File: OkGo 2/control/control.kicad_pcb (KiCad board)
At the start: 2 copper layers, 92.2 x 64.5 mm, 69 parts, among them M3_MOUNT VAL**, P102 KEYSW, P105 BATT, P106 ARM_LED, P108 SMA, P110 POWER_SW, P111 SERIAL, P201 CH1, P202 CH2, P205 CH3, P206 CH4, Q201 BSS138BK, Q202 BSS138BK, Q203 BSS138BK, Q204 BSS138BK, U101 SWD, U102 STM32F071CBT6, U103 MEJ2S0305SC, U105 RFM95W, U106 LCD_HD44780, U107 ADP3335, Y101 8MHz

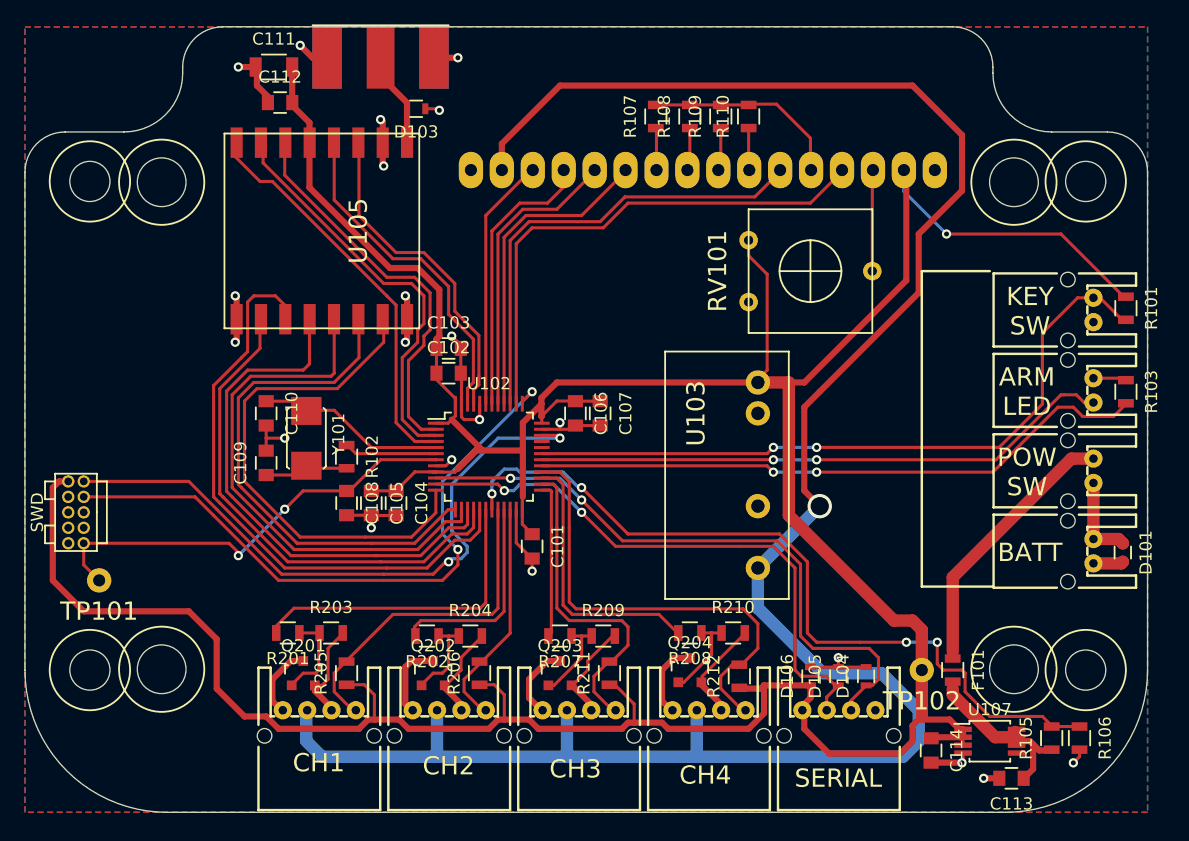
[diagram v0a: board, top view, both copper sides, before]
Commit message: Fixed #28 on control
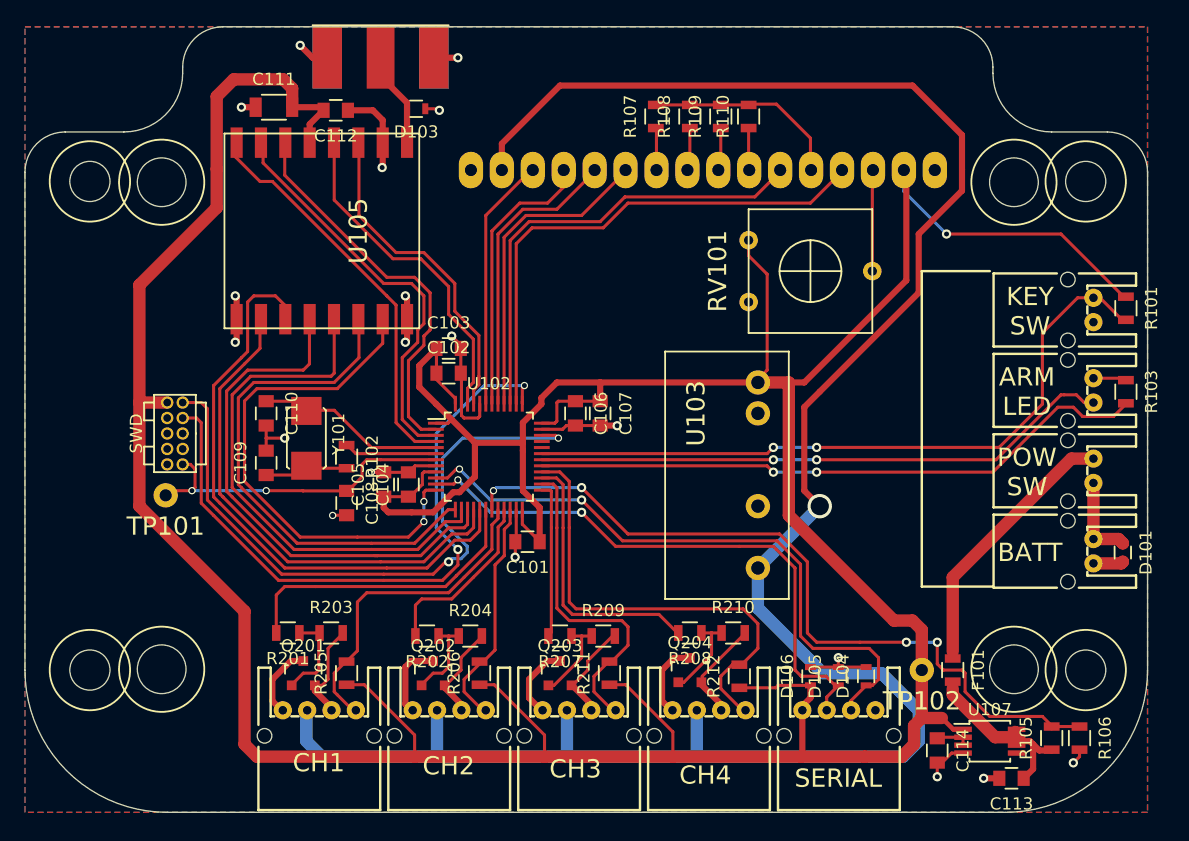
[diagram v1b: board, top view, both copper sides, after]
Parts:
- moved U101 10.4 mm to (145.5, 98.4)
- moved TP101 8.87 mm to (144.1, 106.0)
- moved C112 4.62 mm to (158.1, 74.4), turned to 180 degrees
- moved C111 3.30 mm to (153.0, 74.2)
- moved C104 1.83 mm to (164.1, 105.2), turned to 90 degrees
- moved C105 1.83 mm to (162.1, 105.2), turned to 90 degrees
- moved C101 0.54 mm to (173.9, 109.9), turned to 180 degrees
- moved C114 0.51 mm to (207.5, 127.0)
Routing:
- net +3V3: track 313.8 -> 360.6 mm
- net /nRST: track 36.4 -> 27.4 mm
- net /controls/CH2_LED: track 17.0 -> 15.1 mm
- net /BATT_MON: track 65.9 -> 64.4 mm
- net /SWDCLK: track 53.2 -> 54.7 mm
- net /SWDIO: track 53.6 -> 54.6 mm
- net /controls/CH1_SW: track 27.8 -> 27.1 mm
- net /controls/CH1_LED: track 26.3 -> 25.6 mm
- net /RFM_DIO5: track 42.5 -> 43.1 mm, vias 0 -> 2
- net Net-(D104-Pad1): track 51.5 -> 52.1 mm
- net GND: track 119.3 -> 118.8 mm, vias 21 -> 19

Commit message: Tidied control 3v3,5 fixes #38
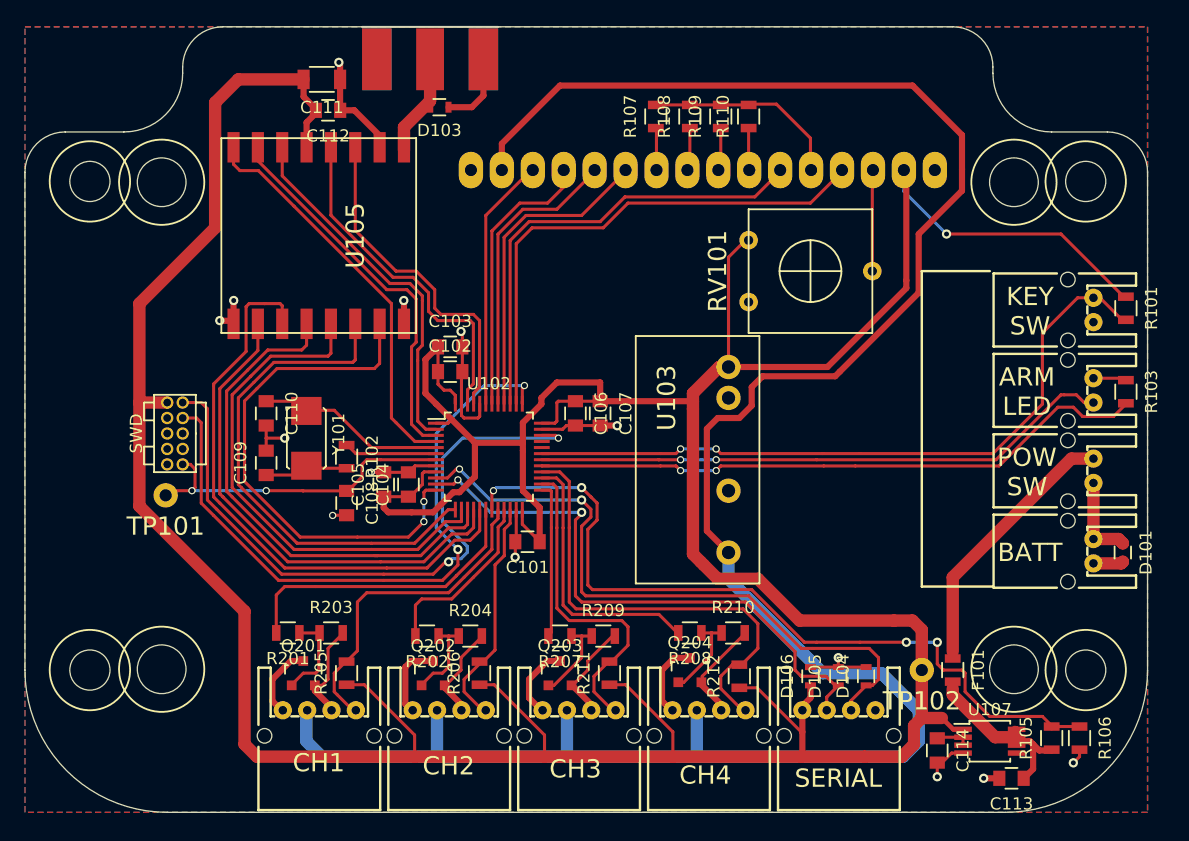
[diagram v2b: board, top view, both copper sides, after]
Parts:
- moved C111 4.55 mm to (157.0, 71.9), turned to 180 degrees
- moved P108 4.07 mm to (165.9, 70.2)
- moved U103 2.73 mm to (190.4, 95.5)
- moved D103 1.91 mm to (166.6, 74.2)
- moved C112 0.64 mm to (157.5, 74.4)
- moved U105 0.46 mm to (156.7, 84.7)
- moved C103 0.18 mm to (167.5, 93.9)
- moved C102 0.18 mm to (167.5, 95.9)
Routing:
- net +3V3: track 360.6 -> 368.4 mm
- net +5V: track 175.2 -> 182.8 mm, vias 1 -> 0
- net /RFM_DIO0: track 32.7 -> 29.9 mm
- net /RFM_DIO1: track 33.4 -> 31.4 mm
- net /RFM_NSS: track 44.3 -> 42.7 mm
- net /BATT_MON: track 64.4 -> 66.0 mm
- net Net-(D104-Pad1): track 52.1 -> 53.7 mm
- net /RFM_SCK: track 44.4 -> 42.9 mm
- net GND: track 118.8 -> 117.6 mm, vias 19 -> 14
- net /RFM_DIO2: track 33.5 -> 32.7 mm
- net /RFM_DIO3: track 27.0 -> 27.8 mm
- net /RFM_MOSI: track 49.1 -> 48.4 mm
- net Net-(D105-Pad1): track 47.5 -> 48.3 mm
- net Net-(D103-Pad2): track 8.19 -> 8.88 mm
- net /RFM_RESET: track 42.8 -> 42.2 mm

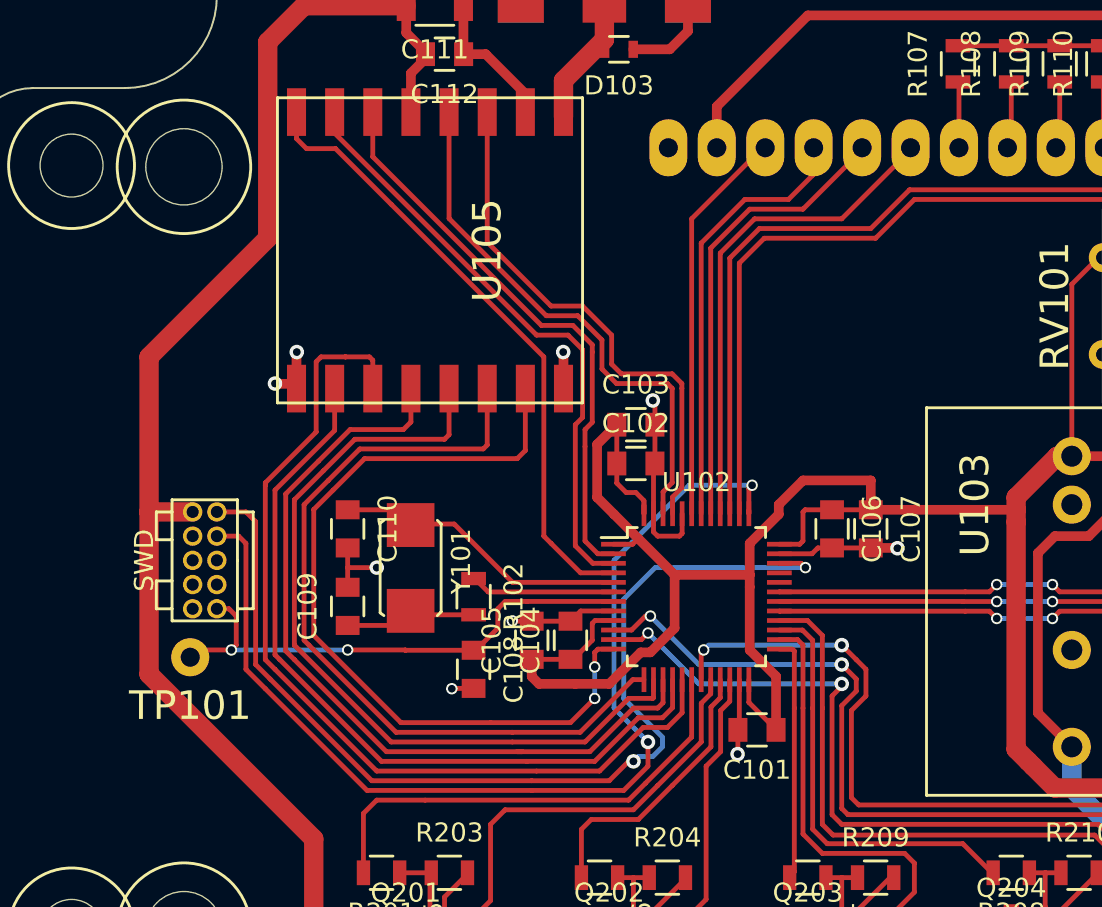
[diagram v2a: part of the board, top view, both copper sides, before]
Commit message: Moved control SWD, resolves #29
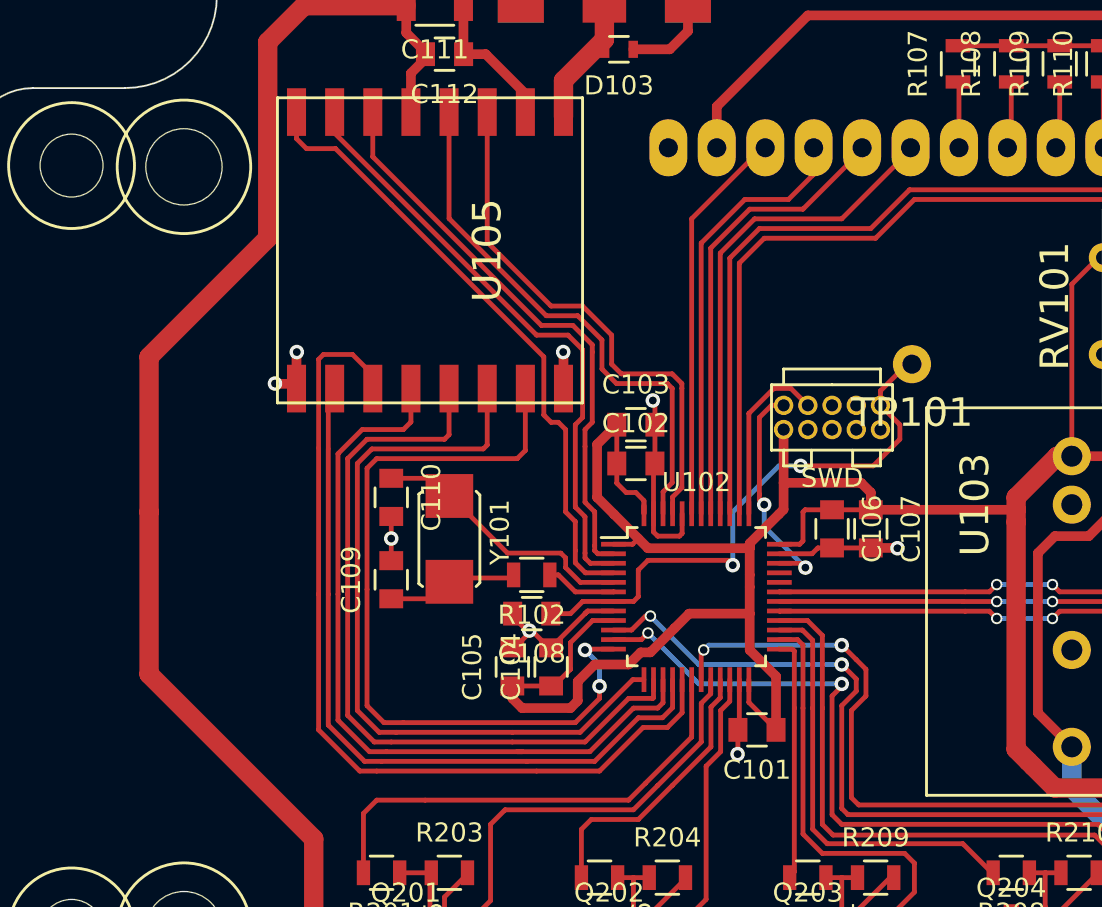
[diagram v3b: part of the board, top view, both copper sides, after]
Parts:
- moved TP101 40.8 mm to (182.0, 90.7)
- moved U101 30.2 mm to (175.3, 92.8), turned to 0 degrees
- moved C108 4.22 mm to (162.1, 103.8), turned to 180 degrees
- moved R102 3.26 mm to (162.1, 101.7), turned to 180 degrees
- moved C110 2.82 mm to (154.7, 97.7)
- moved C109 2.68 mm to (154.7, 102.0)
- moved Y101 2.54 mm to (157.7, 97.8)
- moved C104 1.73 mm to (163.1, 106.6)
- moved C105 1.73 mm to (161.0, 106.6)
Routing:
- net /SWDCLK: track 54.7 -> 9.26 mm, vias 2 -> 0
- net /SWDIO: track 54.6 -> 11.9 mm
- net +3V3: track 368.4 -> 373.9 mm
- net Net-(R102-Pad1): track 7.75 -> 3.74 mm
- net /nRST: track 27.4 -> 29.9 mm
- net /RFM_MOSI: track 48.4 -> 46.3 mm
- net /RFM_NSS: track 42.7 -> 40.5 mm
- net /RFM_RESET: track 42.2 -> 40.0 mm
- net /RFM_SCK: track 42.9 -> 40.7 mm
- net Net-(C110-Pad1): track 16.1 -> 14.2 mm
- net /RFM_MISO: track 41.3 -> 39.5 mm
- net Net-(C109-Pad1): track 8.16 -> 6.94 mm
- net /RFM_DIO5: track 43.1 -> 42.1 mm
- net GND: track 117.6 -> 117.7 mm, vias 14 -> 13

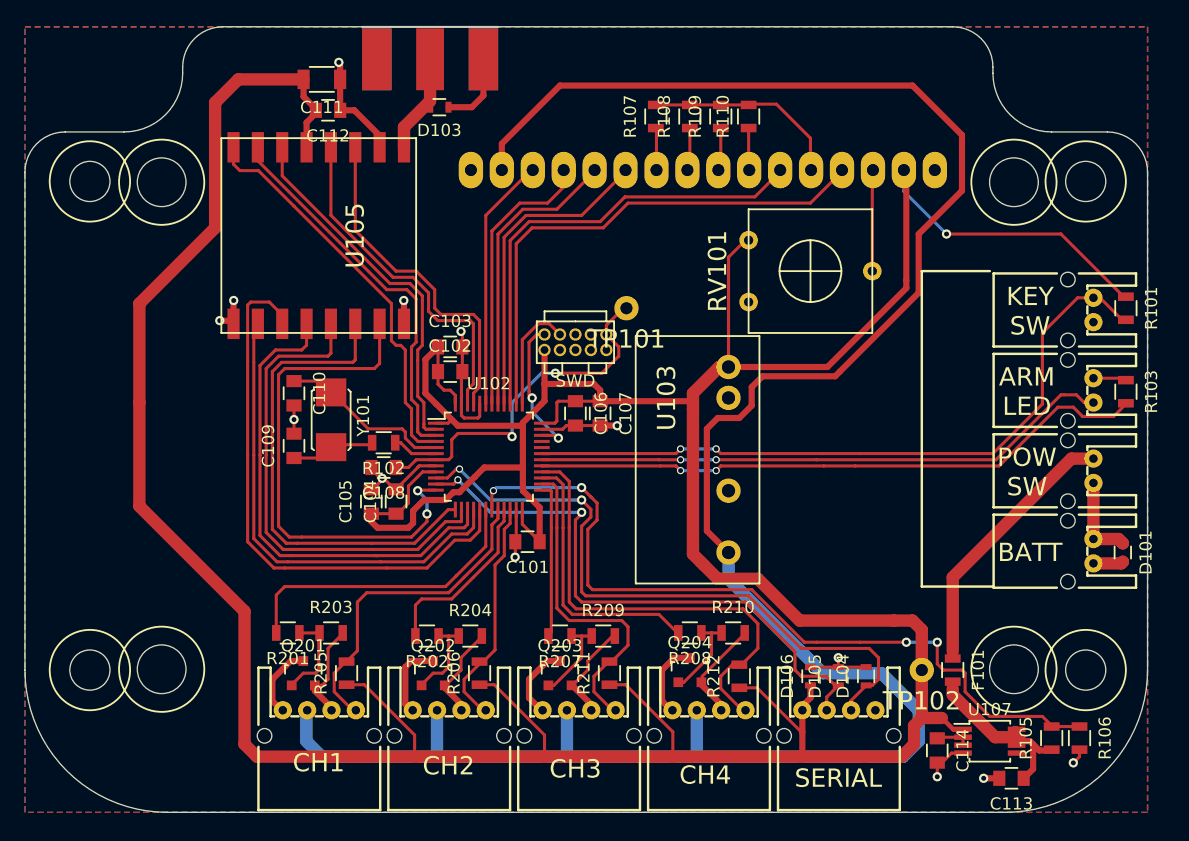
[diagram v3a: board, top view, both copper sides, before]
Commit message: Corrected a bunch of footprints, see #9
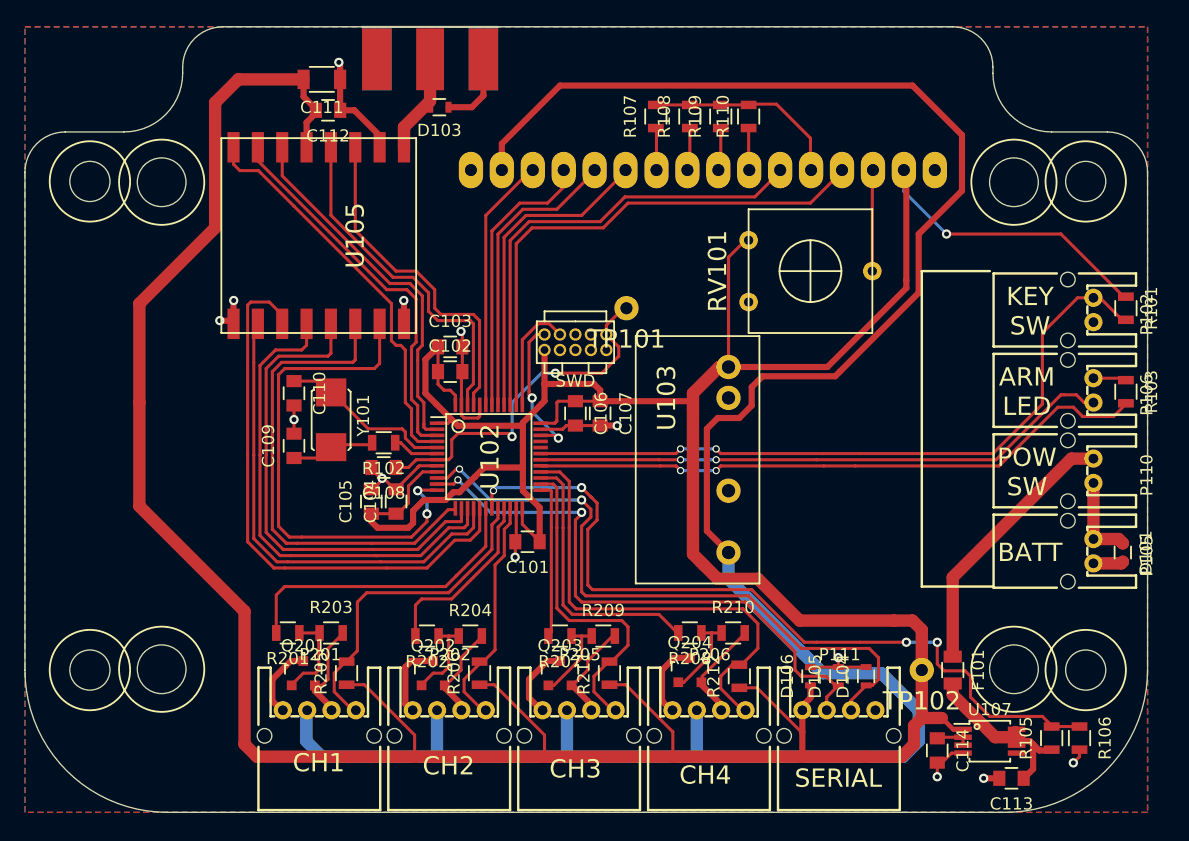
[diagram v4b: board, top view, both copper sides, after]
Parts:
- F101: footprint Resistors_SMD:R_0805 -> control:polyfuse0805
- U102: footprint Housings_QFP:LQFP-48_7x7mm_Pitch0.5mm -> common:LQFP48_ST
- U107: footprint Housings_SSOP:MSOP-8_3x3mm_Pitch0.65mm -> control:MSOP-8_3x3mm_Pitch0.65mm
- turned U102 to 270 degrees

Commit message: More footprints, partial #9
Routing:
- net GND: track 117.7 -> 130.3 mm, vias 13 -> 17
